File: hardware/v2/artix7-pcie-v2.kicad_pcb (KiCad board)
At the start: 4 copper layers, 60 x 51 mm, 191 parts, among them J1 Conn_02x20_Odd_Even, J10 USB_B_Micro, J2 Conn_02x20_Odd_Even, J3 JTAG_EN, J4 USB3_A, J5 USB3_A_AS_PCIE, J6 JTAG, J7 Conn_01x02, J8 SER, SW1 PROG, SW2 USER, U1 XC7A75T-FGG484, U2 W25Q64JVSSIM, U3 LP5907MFX, U4 5P49V6965A000NLGI, U5 TPS82130SILT, U6 TPS82150SILT, U7 TPS82150SILT, U8 TPS82130SILT, U9 TPS82150SILT, X1 25MHz/10pF

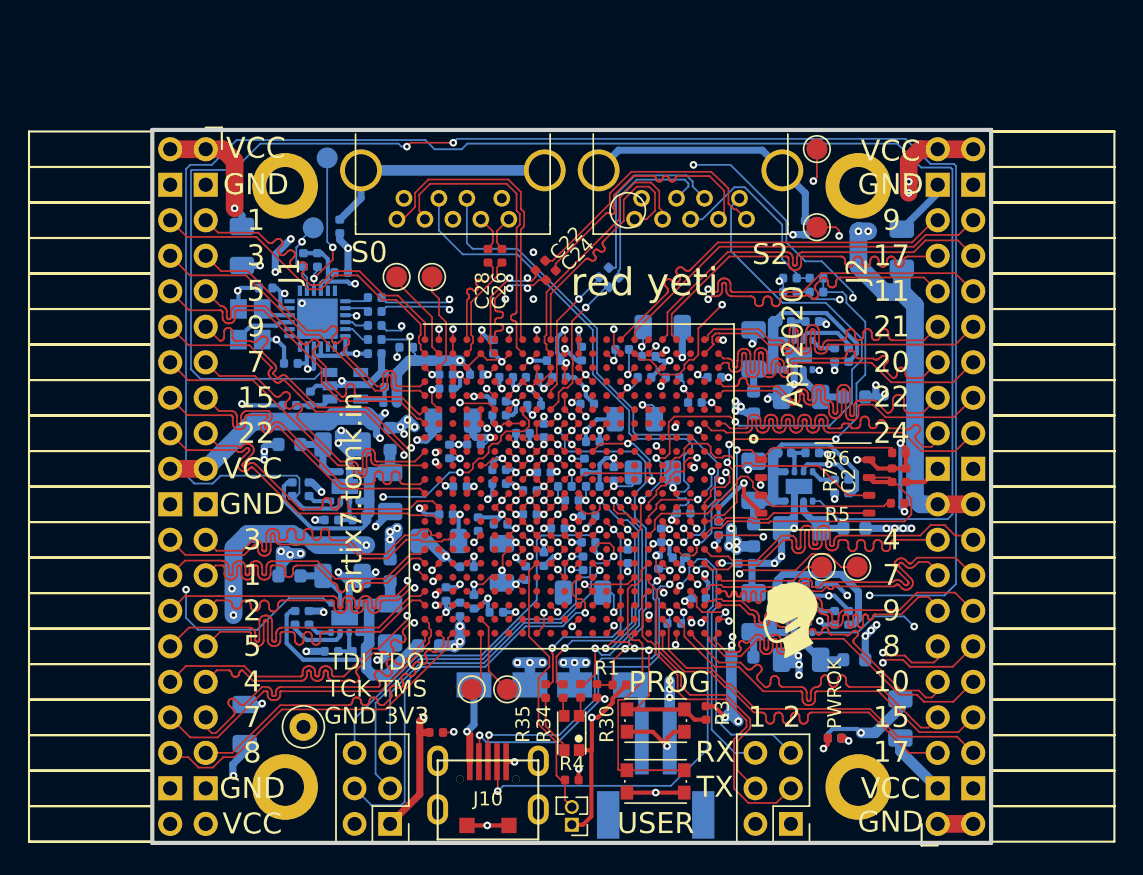
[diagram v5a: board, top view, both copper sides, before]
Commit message: v2 hardware: april 2020 rc2 - add teardrops
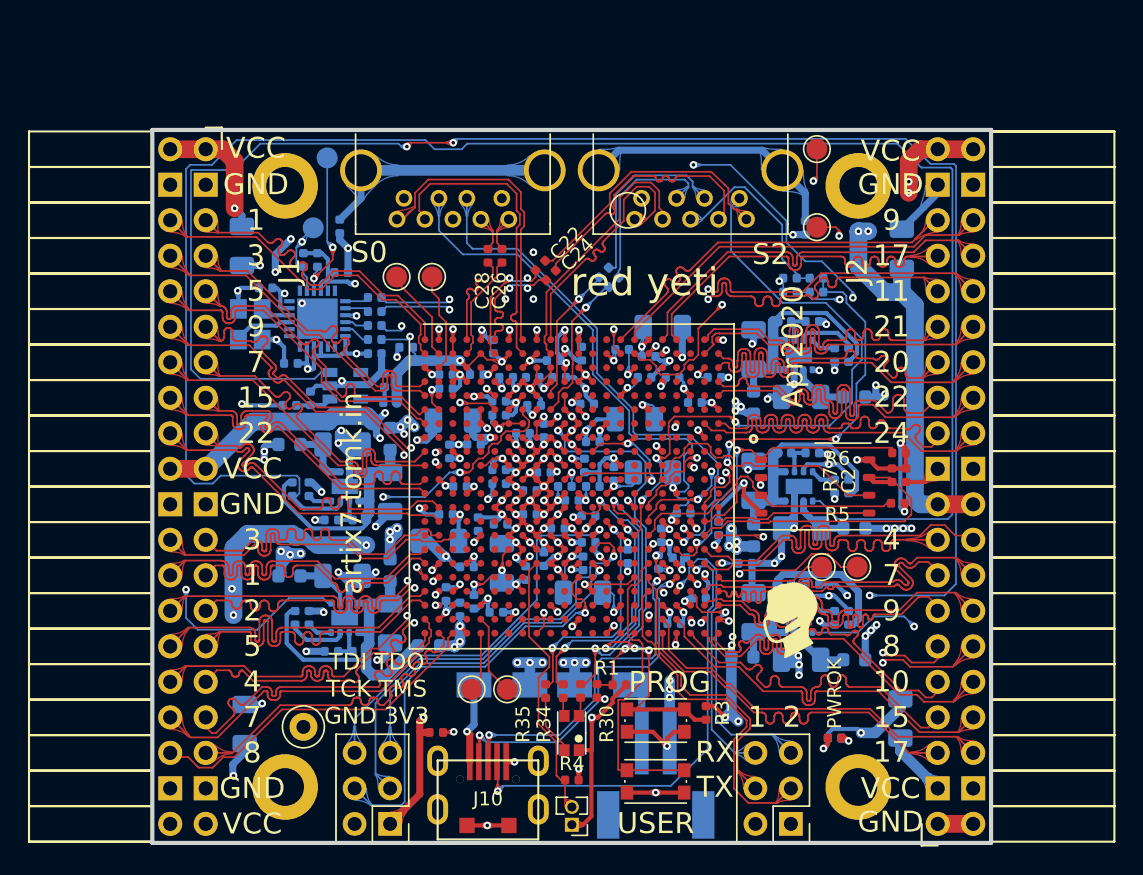
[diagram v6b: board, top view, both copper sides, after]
